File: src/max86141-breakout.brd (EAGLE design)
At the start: 18 x 14 mm, 11 parts, among them J1 1x05 MALE VERT, J2 1x05 MALE VERT, U1 MAX86141ENP+T

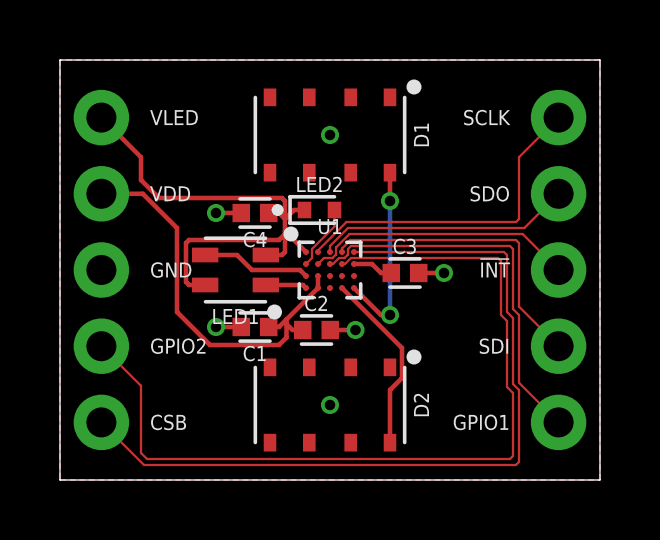
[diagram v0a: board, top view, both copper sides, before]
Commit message: [Rev 1] - Rearrange components from Chih's feedback.  Moved IC out of the way and placed the LEDs symmetrically between the photodiodes.
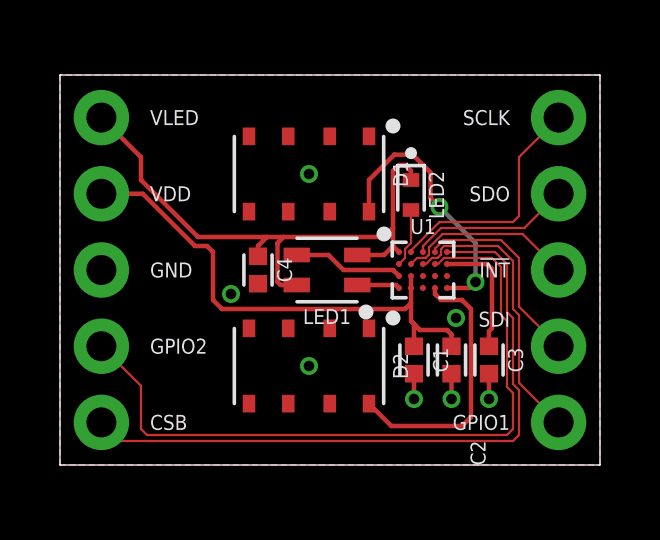
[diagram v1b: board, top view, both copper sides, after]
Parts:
- moved C1 5.41 mm to (2.80, -3.00), turned to 270 degrees
- moved C2 4.61 mm to (4.05, -3.00), turned to 270 degrees
- moved C3 4.03 mm to (5.30, -3.00), turned to 270 degrees
- moved U1 3.10 mm to (3.10, 0.00)
- moved LED2 3.09 mm to (2.70, 2.50), turned to 270 degrees
- moved LED1 3.05 mm to (-0.10, 0.00)
- moved C4 1.90 mm to (-2.40, 0.00), turned to 270 degrees
- moved D1 1.48 mm to (-0.70, 3.20)
- moved D2 1.48 mm to (-0.70, -3.20)
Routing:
- net GPIO2: track 28.7 -> 23.8 mm
- net CSB: track 26.8 -> 22.3 mm
- net SDI: track 10.2 -> 6.77 mm
- net GPIO1: track 12.9 -> 9.57 mm
- net VDD: track 13.8 -> 17.1 mm
- net SCLK: track 11.1 -> 7.95 mm
- net SDO: track 8.54 -> 5.44 mm
- net !INT!: track 9.07 -> 5.97 mm
- net N$1: track 6.15 -> 9.04 mm
- net N$6: track 1.37 -> 4.19 mm
- net N$2: track 6.32 -> 9.01 mm
- net VLED: track 17.9 -> 20.1 mm
- net GND: track 3.37 -> 2.53 mm, vias 6 -> 7
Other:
- board size 18 x 14 mm -> 18 x 13 mm
